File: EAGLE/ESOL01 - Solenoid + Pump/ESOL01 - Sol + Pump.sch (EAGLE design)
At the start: 7 parts, among them J1 ECAM02, J2 SOL1, J3 SOL2, J4 SOL3, J5 SOL4, J6 PUMP

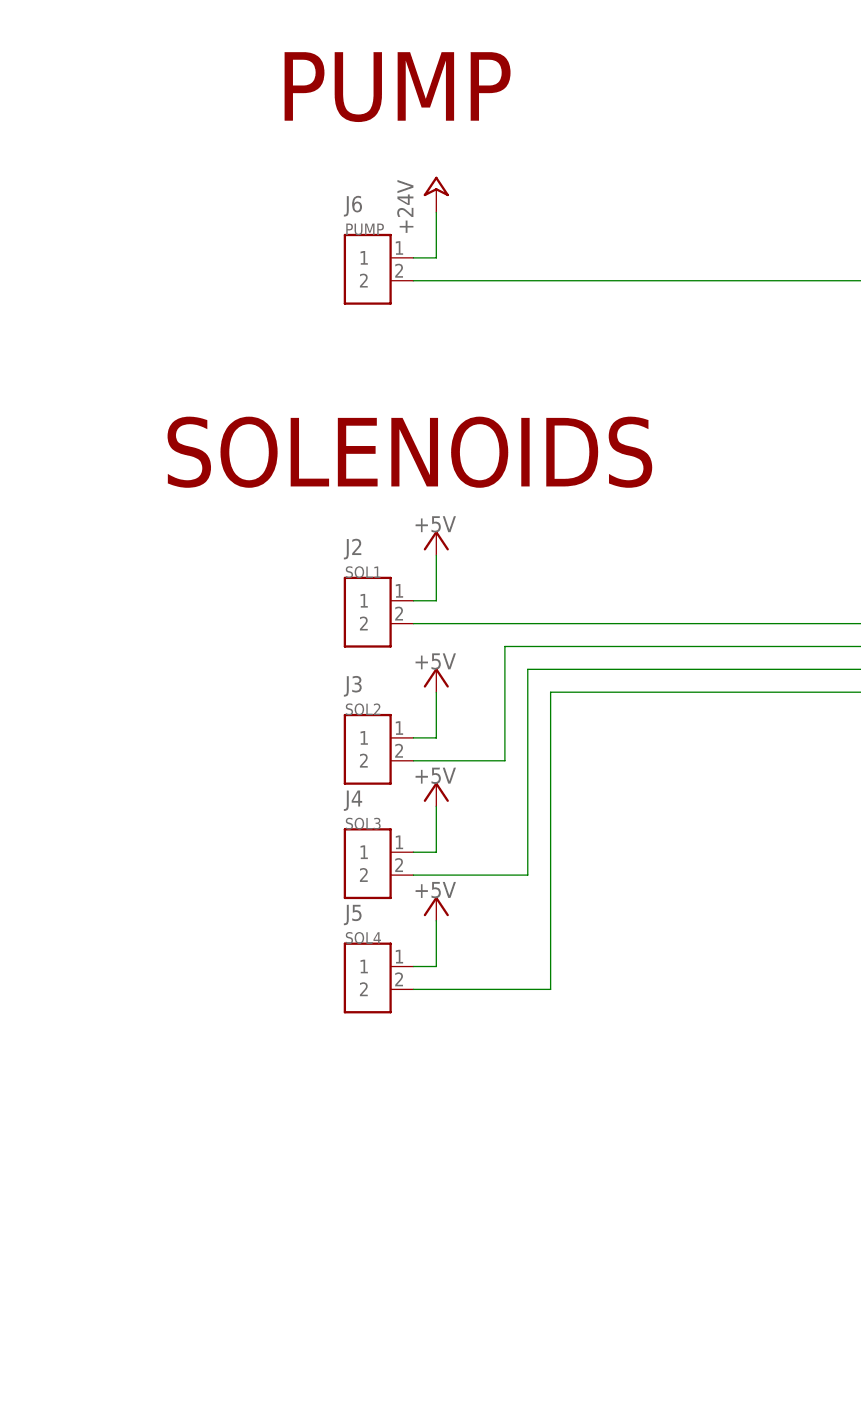
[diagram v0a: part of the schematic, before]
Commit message: Routed ESOL01, created MTHOLE(M3) part for future use
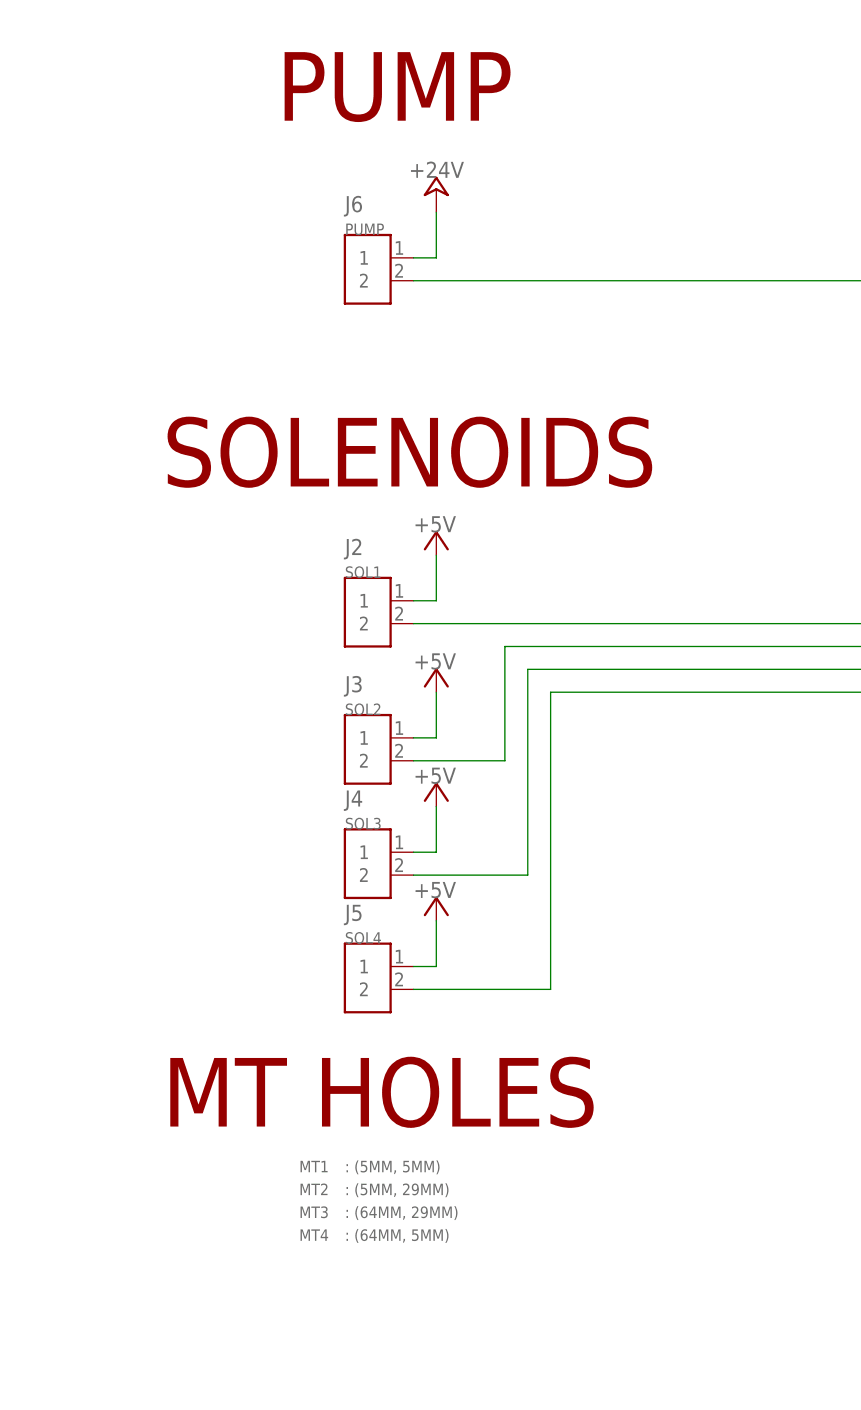
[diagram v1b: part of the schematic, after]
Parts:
- added MT1: : (5MM, 5MM), TinWhiskers:MTHOLE(M3)
- added MT2: : (5MM, 29MM), TinWhiskers:MTHOLE(M3)
- added MT3: : (64MM, 29MM), TinWhiskers:MTHOLE(M3)
- added MT4: : (64MM, 5MM), TinWhiskers:MTHOLE(M3)
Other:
- note added: "MT HOLES"
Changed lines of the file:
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@@
 <part name="P+7" library="supply1" deviceset="+24V" device=""/>
 <part name="LOGO2" library="FirePick" deviceset="LOGO-FIREPICK" device="LARGE"/>
+<part name="MT1" library="TinWhiskers" deviceset="MTHOLE(M3)" device="" value=": (5MM, 5MM)"/>
+<part name="MT2" library="TinWhiskers" deviceset="MTHOLE(M3)" device="" value=": (5MM, 29MM)"/>
+<part name="MT3" library="TinWhiskers" deviceset="MTHOLE(M3)" device="" value=": (64MM, 29MM)"/>
+<part name="MT4" library="TinWhiskers" deviceset="MTHOLE(M3)" device="" value=": (64MM, 5MM)"/>
 </parts>
 <sheets>
@@
 <text x="292.1" y="17.78" size="1.778" layer="94" ratio="15">APPROVED BY: NEIL JANSEN</text>
 <text x="292.1" y="10.16" size="2.54" layer="94" ratio="10">REVISION:</text>
+<text x="35.56" y="63.5" size="7.62" layer="94">MT HOLES</text>
 </plain>
 <instances>
@@
 </instance>
 <instance part="P+7" gate="1" x="66.04" y="167.64" smashed="yes">
-<attribute name="VALUE" x="63.5" y="162.56" size="1.778" layer="96" rot="R90"/>
+<attribute name="VALUE" x="62.992" y="168.91" size="1.778" layer="96"/>
 </instance>
 <instance part="LOGO2" gate="G$1" x="91.44" y="10.16"/>
+<instance part="MT1" gate="G$1" x="55.88" y="58.42" smashed="yes">
+<attribute name="VALUE" x="55.88" y="58.42" size="1.27" layer="96"/>
+<attribute name="NAME" x="50.8" y="58.42" size="1.27" layer="95"/>
+</instance>
+<instance part="MT2" gate="G$1" x="55.88" y="55.88" smashed="yes">
+<attribute name="VALUE" x="55.88" y="55.88" size="1.27" layer="96"/>
+<attribute name="NAME" x="50.8" y="55.88" size="1.27" layer="95"/>
+</instance>
+<instance part="MT3" gate="G$1" x="55.88" y="53.34" smashed="yes">
+<attribute name="VALUE" x="55.88" y="53.34" size="1.27" layer="96"/>
+<attribute name="NAME" x="50.8" y="53.34" size="1.27" layer="95"/>
+</instance>
+<instance part="MT4" gate="G$1" x="55.88" y="50.8" smashed="yes">
+<attribute name="VALUE" x="55.88" y="50.8" size="1.27" layer="96"/>
+<attribute name="NAME" x="50.8" y="50.8" size="1.27" layer="95"/>
+</instance>
 </instances>
 <busses>

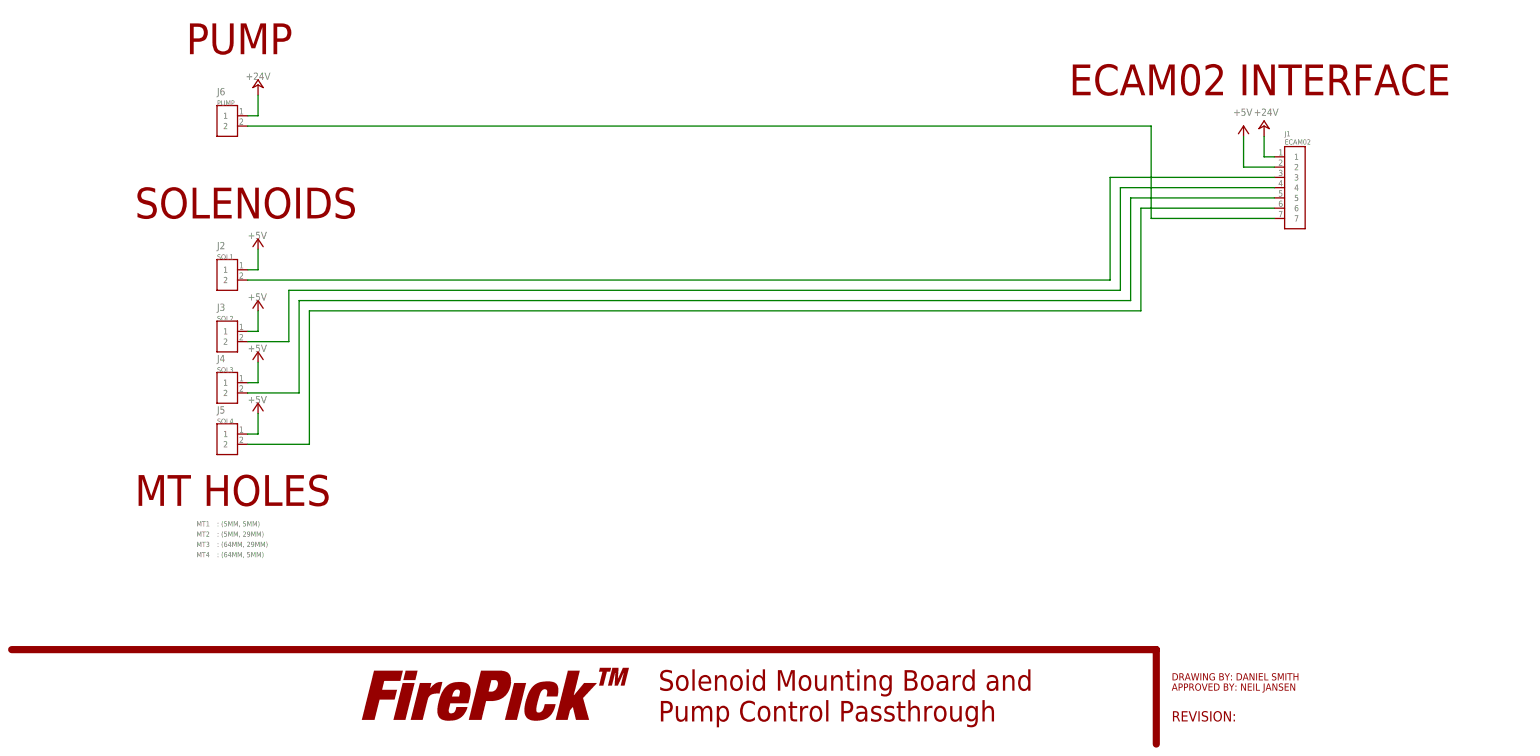
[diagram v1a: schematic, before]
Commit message: Made REV 2 modifications, including increasing width of power traces, adding vias to power traces, and addition of LEDs to all modular tools. Catch diodes added to ESOL01 board to prevent coils from creating problems "upstream"
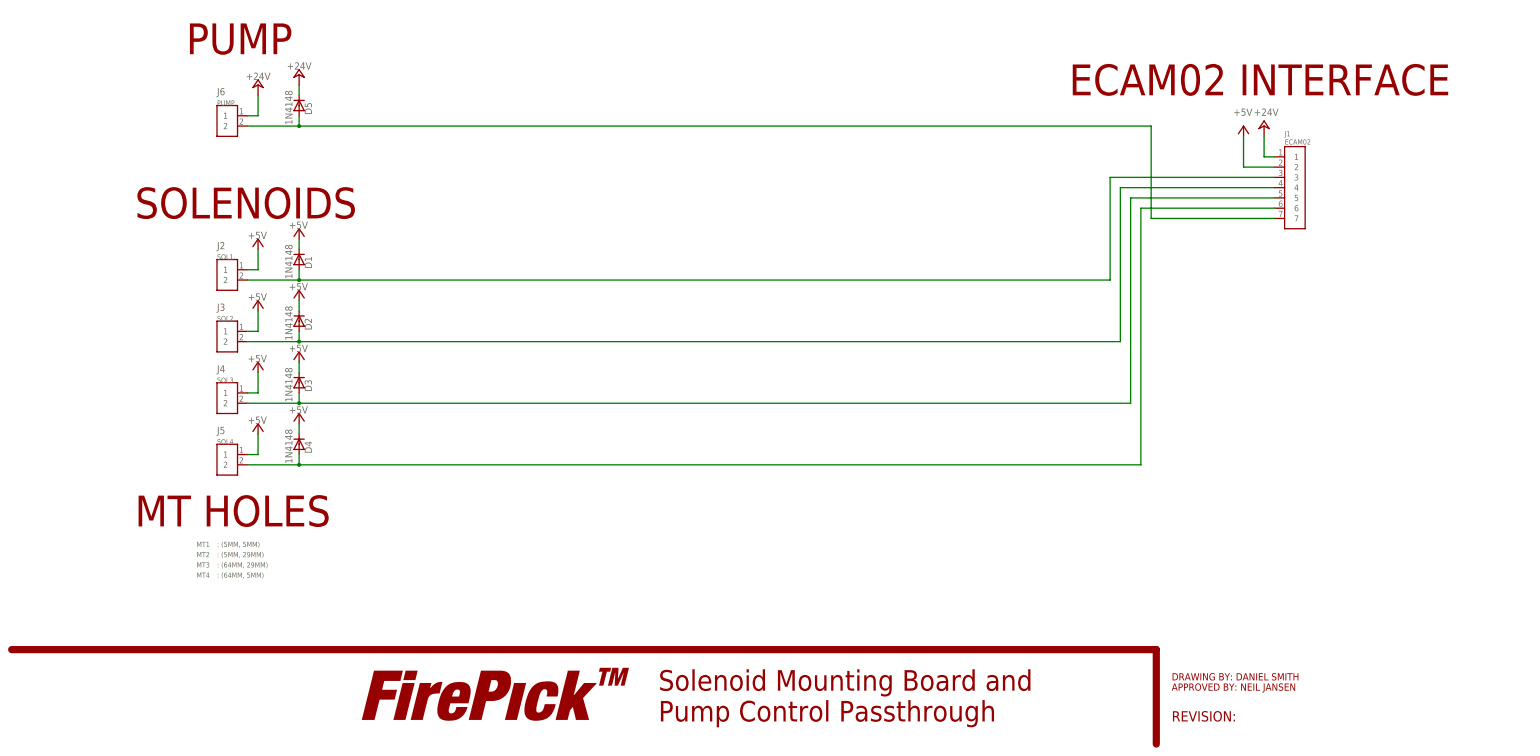
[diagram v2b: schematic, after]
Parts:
- added D1, D2, D3, D4, D5: 1N4148, TinWhiskers:CPL-DIO-1N4148SOD-323
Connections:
- net +24V: now also D5.C
- net +5V: now also D1.C, D2.C, D3.C, D4.C
- net N$10: now also D4.A
- net N$11: now also D5.A
- net N$7: now also D1.A
- net N$8: now also D2.A
- net N$9: now also D3.A
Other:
- moved on the sheet: J4, J5
